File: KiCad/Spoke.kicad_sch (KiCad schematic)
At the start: 130 parts, among them J1 B2B-PH-K-S, J10 BL-A, J11 BL-C, J12 Amphenol 132289, J2 BAT+, J3 BAT-, J4 GCT USB4105/USB4110, J5 CHG+, J6 CHG-, J7 PLS-1x3, J8 PLS-1x6, J9 PLS-1x3, Q1 AO3407A, Q2 AO3400, Q3 AO3400, Q4 AO3400, SW1 PWR, SW2 OK/UP, SW3 ESC/DN, SW4 OK/UP, SW5 ESC/DN, SW6 BOOT, U1 SP0503BAHTG, U2 TP4056, U3 CP2102N-A02-GQFN28, U4 LM3671MF-3.3, U5 74HC4052PW, U6 STM32F103C8T6, U7 LSM303DLHC, X1 8MHz

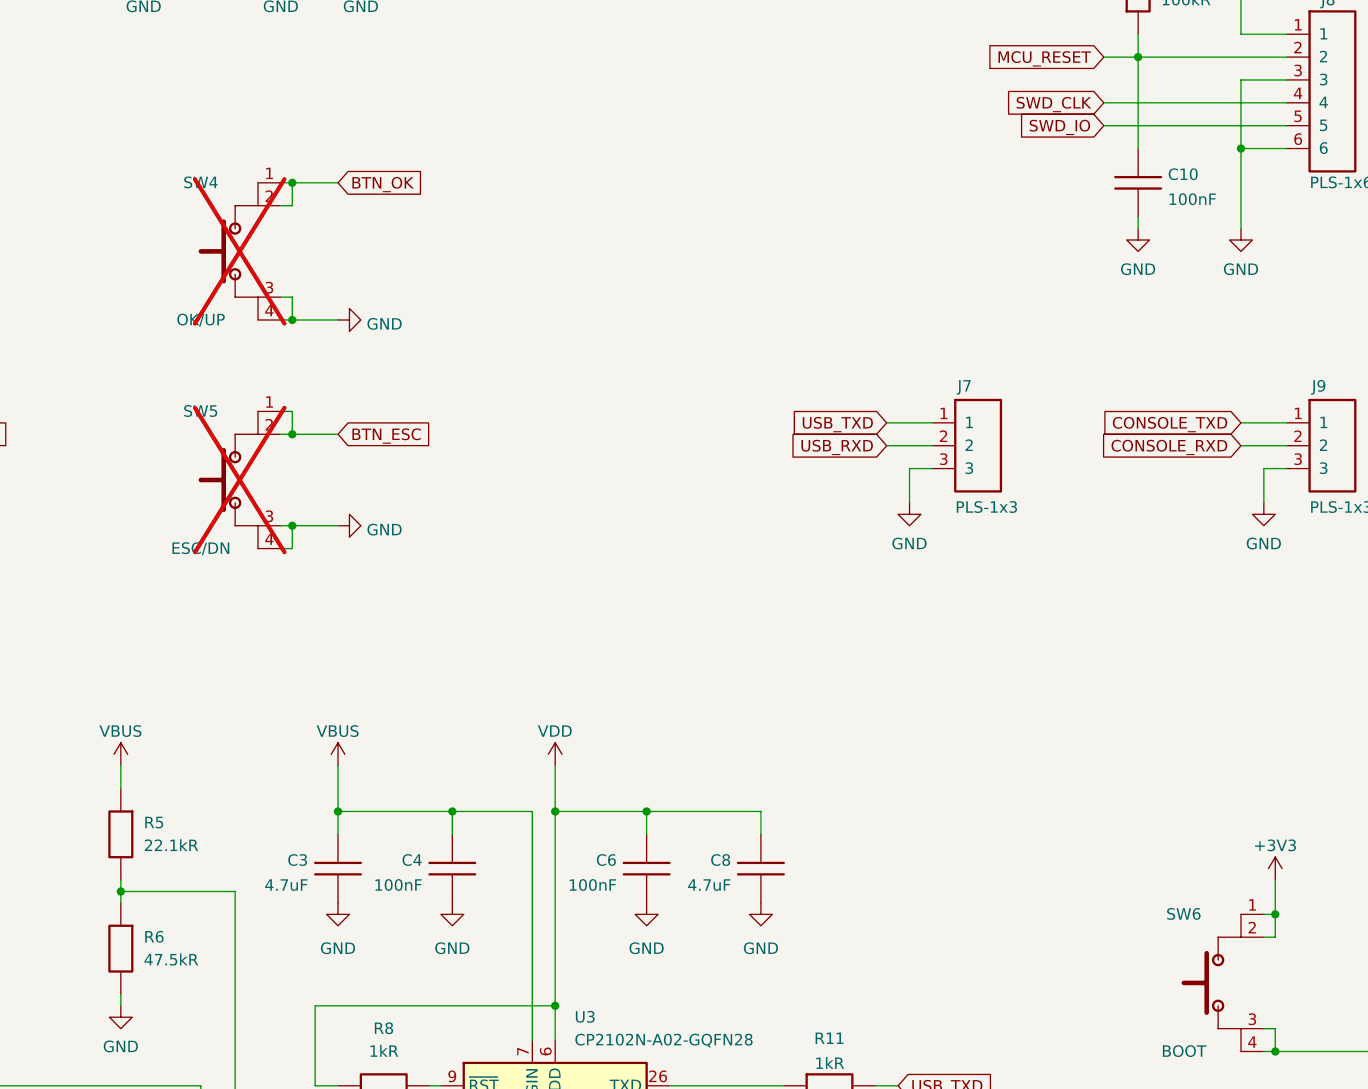
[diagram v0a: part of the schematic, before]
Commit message: Remove unused switches, arrangement
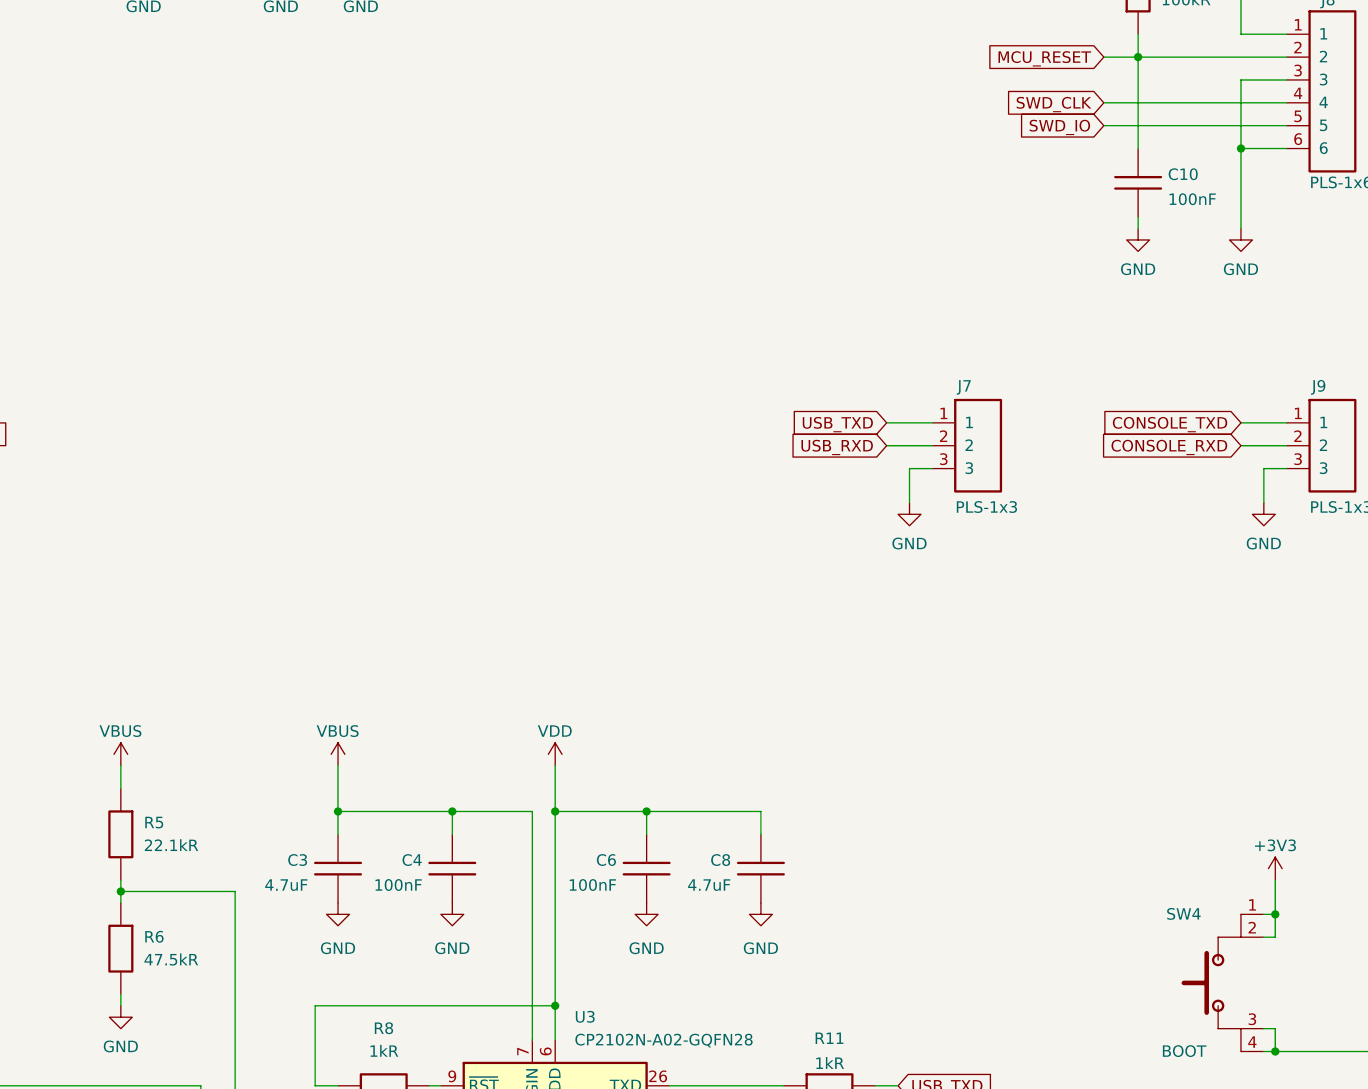
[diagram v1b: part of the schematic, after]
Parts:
- removed SW4: OK/UP, Spoke:Button_6x6, symbol Spoke:Button-SPST-NO
- removed SW5: ESC/DN, Spoke:Button_6x6, symbol Spoke:Button-SPST-NO
- renumbered SW6 to SW4

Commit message: Replace LEDs by 3 mm
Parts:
- D2, D3, D4: footprint Spoke:LED1206 -> Spoke:LED_3mm
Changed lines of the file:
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@@
 			)
 		)
-		(property "Footprint" "Spoke:LED1206"
+		(property "Footprint" "Spoke:LED_3mm"
 			(at 346.71 203.2 0)
 			(effects
@@
 			)
 		)
-		(property "Footprint" "Spoke:LED1206"
+		(property "Footprint" "Spoke:LED_3mm"
 			(at 134.62 349.25 0)
 			(effects
@@
 			)
 		)
-		(property "Footprint" "Spoke:LED1206"
+		(property "Footprint" "Spoke:LED_3mm"
 			(at 346.71 215.9 0)
 			(effects

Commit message: Start routing
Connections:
- net at J4.A7 (D-), J4.B7 (D-), U3.5 (D-): now also U1.3 (K); no longer U1.2 (K)
- net at J4.A6 (D+), J4.B6 (D+), U3.4 (D+): now also U1.2 (K); no longer U1.3 (K)
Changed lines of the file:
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@@
 	)
 	(junction
-		(at 95.25 246.38)
-		(diameter 0)
-		(color 0 0 0 0)
-	)
-	(junction
 		(at 298.45 45.72)
 		(diameter 0)
@@
 	)
 	(junction
+		(at 95.25 243.84)
+		(diameter 0)
+		(color 0 0 0 0)
+	)
+	(junction
 		(at 331.47 60.96)
 		(diameter 0)
@@
 	)
 	(junction
-		(at 92.71 243.84)
-		(diameter 0)
-		(color 0 0 0 0)
-	)
-	(junction
 		(at 115.57 88.9)
 		(diameter 0)
@@
 		(color 0 0 0 0)
 	)
+	(junction
+		(at 92.71 246.38)
+		(diameter 0)
+		(color 0 0 0 0)
+	)
 	(no_connect
 		(at 149.86 289.56)
@@
 	(wire
 		(pts
-			(xy 62.23 243.84) (xy 92.71 243.84)
-		)
-		(stroke
-			(width 0)
-			(type default)
-		)
-	)
-	(wire
-		(pts
 			(xy 488.95 194.31) (xy 492.76 194.31)
 		)
@@
 	(wire
 		(pts
-			(xy 95.25 246.38) (xy 124.46 246.38)
+			(xy 62.23 246.38) (xy 92.71 246.38)
 		)
 		(stroke
@@
 	(wire
 		(pts
-			(xy 92.71 243.84) (xy 92.71 251.46)
-		)
-		(stroke
-			(width 0)
-			(type default)
-		)
-	)
-	(wire
-		(pts
 			(xy 85.09 349.25) (xy 97.79 349.25)
 		)
@@
 	(wire
 		(pts
-			(xy 95.25 246.38) (xy 95.25 251.46)
-		)
-		(stroke
-			(width 0)
-			(type default)
-		)
-	)
-	(wire
-		(pts
 			(xy 339.09 132.08) (xy 339.09 134.62)
 		)
@@
 	(wire
 		(pts
-			(xy 62.23 246.38) (xy 95.25 246.38)
-		)
-		(stroke
-			(width 0)
-			(type default)
-		)
-	)
-	(wire
-		(pts
 			(xy 129.54 374.65) (xy 129.54 369.57)
 		)
@@
 	(wire
 		(pts
+			(xy 92.71 246.38) (xy 124.46 246.38)
+		)
+		(stroke
+			(width 0)
+			(type default)
+		)
+	)
+	(wire
+		(pts
 			(xy 459.74 182.88) (xy 459.74 212.09)
 		)
@@
 	(wire
 		(pts
-			(xy 92.71 243.84) (xy 124.46 243.84)
+			(xy 62.23 243.84) (xy 95.25 243.84)
 		)
 		(stroke
@@
 	(wire
 		(pts
+			(xy 92.71 246.38) (xy 92.71 251.46)
+		)
+		(stroke
+			(width 0)
+			(type default)
+		)
+	)
+	(wire
+		(pts
 			(xy 354.33 71.12) (xy 358.14 71.12)
 		)
@@
 	(wire
 		(pts
+			(xy 95.25 243.84) (xy 95.25 251.46)
+		)
+		(stroke
+			(width 0)
+			(type default)
+		)
+	)
+	(wire
+		(pts
 			(xy 48.26 50.8) (xy 48.26 45.72)
 		)
@@
 		)
 		(stroke
+			(width 0)
+			(type default)
+		)
+	)
+	(wire
+		(pts
+			(xy 95.25 243.84) (xy 124.46 243.84)
+		)
+		(stroke

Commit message: Replace DCDC caps by Ceramic 10 uF
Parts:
- removed C13, C7: 47uF, Spoke:C_tantA, symbol Spoke:C-Polar
- added C13, C7: 10uF, Spoke:C1206, symbol Spoke:C
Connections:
- net +3V3: now also C13.2
- net GND: now also C13.1, C7.1
- net VCC: now also C7.2
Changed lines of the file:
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@@
 	)
 	(symbol
-		(lib_id "Spoke:C-Polar")
-		(at 158.75 52.07 270)
+		(lib_id "power:GND")
+		(at 39.37 269.24 0)
 		(unit 1)
 		(exclude_from_sim no)
@@
 		(dnp no)
 		(fields_autoplaced yes)
-		(property "Reference" "C7"
-			(at 163.83 53.7209 90)
+		(property "Reference" "#PWR01"
+			(at 39.37 275.59 0)
 			(effects
 				(font
 					(size 1.27 1.27)
 				)
-				(justify left)
+				(hide yes)
 			)
 		)
-		(property "Value" "47uF"
-			(at 163.83 56.2609 90)
+		(property "Value" "GND"
+			(at 39.37 273.8025 0)
 			(effects
 				(font
 					(size 1.27 1.27)
 				)
-				(justify left)
 			)
 		)
-		(property "Footprint" "Spoke:C_tantA"
-			(at 171.45 52.07 0)
+		(property "Footprint" ""
+			(at 39.37 269.24 0)
 			(effects
 				(font
@@
 		)
 		(property "Datasheet" ""
-			(at 171.45 52.07 0)
+			(at 39.37 269.24 0)
 			(effects
 				(font
@@
 		)
 		(property "Description" ""
-			(at 158.75 52.07 0)
+			(at 39.37 269.24 0)
 			(effects
 				(font
 					(size 1.27 1.27)
 				)
-				(hide yes)
 			)
 		)
 		(pin "1"
 		)
-		(pin "2"
-		)
 		(instances
 			(project "Spoke"
 				(path "/e63e39d7-6ac0-4ffd-8aa3-1841a4541b55"
-					(reference "C7")
+					(reference "#PWR01")
 					(unit 1)
 				)
@@
 	)
 	(symbol
-		(lib_id "power:GND")
-		(at 39.37 269.24 0)
+		(lib_id "Spoke:C")
+		(at 158.75 59.69 90)
 		(unit 1)
 		(exclude_from_sim no)
@@
 		(dnp no)
 		(fields_autoplaced yes)
-		(property "Reference" "#PWR01"
-			(at 39.37 275.59 0)
+		(property "Reference" "C7"
+			(at 155.4481 54.9715 90)
 			(effects
 				(font
 					(size 1.27 1.27)
 				)
-				(hide yes)
+				(justify left)
 			)
 		)
-		(property "Value" "GND"
-			(at 39.37 273.8025 0)
+		(property "Value" "10uF"
+			(at 155.4481 57.7466 90)
 			(effects
 				(font
 					(size 1.27 1.27)
 				)
+				(justify left)
 			)
 		)
-		(property "Footprint" ""
-			(at 39.37 269.24 0)
+		(property "Footprint" "Spoke:C1206"
+			(at 146.05 59.69 0)
 			(effects
 				(font
@@
 		)
 		(property "Datasheet" ""
-			(at 39.37 269.24 0)
+			(at 146.05 59.69 0)
 			(effects
 				(font
@@
 		)
 		(property "Description" ""
-			(at 39.37 269.24 0)
+			(at 158.75 59.69 0)
 			(effects
 				(font
@@
 		(pin "1"
 		)
+		(pin "2"
+		)
 		(instances
 			(project "Spoke"
 				(path "/e63e39d7-6ac0-4ffd-8aa3-1841a4541b55"
-					(reference "#PWR01")
+					(reference "C7")
 					(unit 1)
 				)
@@
 	)
 	(symbol
+		(lib_id "Spoke:C")
+		(at 243.84 59.69 90)
+		(unit 1)
+		(exclude_from_sim no)
+		(in_bom yes)
+		(on_board yes)
+		(dnp no)
+		(fields_autoplaced yes)
+		(property "Reference" "C13"
+			(at 240.5381 54.9715 90)
+			(effects
+				(font
+					(size 1.27 1.27)
+				)
+				(justify left)
+			)
+		)
+		(property "Value" "10uF"
+			(at 240.5381 57.7466 90)
+			(effects
+				(font
+					(size 1.27 1.27)
+				)
+				(justify left)
+			)
+		)
+		(property "Footprint" "Spoke:C1206"
+			(at 231.14 59.69 0)
+			(effects
+				(font
+					(size 1.27 1.27)
+				)
+				(hide yes)
+			)
+		)
+		(property "Datasheet" ""
+			(at 231.14 59.69 0)
+			(effects
+				(font
+					(size 1.27 1.27)
+				)
+				(hide yes)
+			)
+		)
+		(property "Description" ""
+			(at 243.84 59.69 0)
+			(effects
+				(font
+					(size 1.27 1.27)
+				)
+			)
+		)
+		(pin "1"
+		)
+		(pin "2"
+		)
+		(instances
+			(project "Spoke"
+				(path "/e63e39d7-6ac0-4ffd-8aa3-1841a4541b55"
+					(reference "C13")
+					(unit 1)
+				)
+			)
+		)
+	)
+	(symbol
 		(lib_id "Spoke:R")
 		(at 236.22 294.64 0)
@@
 					(unit 1)
 				)
-			)
-		)
-	)
-	(symbol
-		(lib_id "Spoke:C-Polar")
-		(at 243.84 52.07 270)
-		(unit 1)
-		(exclude_from_sim no)
-		(in_bom yes)
-		(on_board yes)
-		(dnp no)
-		(fields_autoplaced yes)
-		(property "Reference" "C13"
-			(at 248.92 53.7209 90)
-			(effects
-				(font
-					(size 1.27 1.27)
-				)
-				(justify left)
-			)
-		)
-		(property "Value" "47uF"
-			(at 248.92 56.2609 90)
-			(effects
-				(font
-					(size 1.27 1.27)
-				)
-				(justify left)
-			)
-		)
-		(property "Footprint" "Spoke:C_tantA"
-			(at 256.54 52.07 0)
-			(effects
-				(font
-					(size 1.27 1.27)
-				)
-				(hide yes)
-			)
-		)
-		(property "Datasheet" ""
-			(at 256.54 52.07 0)
-			(effects
-				(font
-					(size 1.27 1.27)
-				)
-				(hide yes)
-			)
-		)
-		(property "Description" ""
-			(at 243.84 52.07 0)
-			(effects
-				(font
-					(size 1.27 1.27)
-				)
-				(hide yes)
-			)
-		)
-		(pin "1"
-		)
-		(pin "2"
-		)
-		(instances
-			(project ""
-				(path "/e63e39d7-6ac0-4ffd-8aa3-1841a4541b55"
-					(reference "C13")
-					(unit 1)
-				)

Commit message: Route USB-UART
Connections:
- net USB_DP: now reaches J4.A6 (D+), J4.B6 (D+), U1.2 (K), U3.4 (D+)
- net USB_DN: now reaches J4.A7 (D-), J4.B7 (D-), U1.3 (K), U3.5 (D-)
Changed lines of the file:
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@@
+		)
+	)
+	(label "USB_DN"
+		(at 101.6 243.84 0)
+		(effects
+			(font
+				(size 1.27 1.27)
+			)
+			(justify left bottom)
 		)
 	)
@@
 		(effects
 			(font
+				(size 1.27 1.27)
+			)
+			(justify left bottom)
+		)
+	)
+	(label "USB_DP"
+		(at 101.6 246.38 0)
+		(effects
+			(font

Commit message: Add C14
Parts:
- added C14: 47uF, Spoke:C_tantA, symbol Spoke:C-Polar
- renumbered C14 to C15, C15 to C16, C16 to C17, C17 to C18, C18 to C19, C19 to C20, C20 to C21, C21 to C22, C22 to C23, C23 to C24, C24 to C25, C25 to C26, C26 to C27, C27 to C28, C28 to C29, C29 to C30, C30 to C31, C31 to C32, C32 to C33
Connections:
- net +3V3: now also C14.1
- net GND: now also C14.2
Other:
- moved on the sheet: C16, C17, C18, C20

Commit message: Add TP1, TP2
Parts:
- added TP1, TP2: Pad-Round, Spoke:Pad_round, symbol Spoke:Pad-Round
- renumbered TP8 to TP10, TP9 to TP11, TP10 to TP12, TP11 to TP13, TP12 to TP14, TP13 to TP15, TP14 to TP16, TP15 to TP17, TP16 to TP18, TP1 to TP3, TP2 to TP4, TP3 to TP5, TP4 to TP6, TP5 to TP7, TP6 to TP8, TP7 to TP9
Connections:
- net MUX_BLE_USB: now also TP2.1
- net VDD: now also TP1.1
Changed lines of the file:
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@@
 	)
 	(junction
+		(at 203.2 334.01)
+		(diameter 0)
+		(color 0 0 0 0)
+	)
+	(junction
 		(at 91.44 58.42)
 		(diameter 0)
@@
 	)
 	(junction
+		(at 160.02 198.12)
+		(diameter 0)
+		(color 0 0 0 0)
+	)
+	(junction
 		(at 414.02 335.28)
 		(diameter 0)
@@
 	(wire
 		(pts
-			(xy 203.2 330.2) (xy 203.2 349.25)
+			(xy 203.2 330.2) (xy 203.2 334.01)
 		)
 		(stroke
@@
 	(wire
 		(pts
+			(xy 201.93 334.01) (xy 203.2 334.01)
+		)
+		(stroke
+			(width 0)
+			(type default)
+		)
+	)
+	(wire
+		(pts
 			(xy 92.71 246.38) (xy 124.46 246.38)
 		)
@@
 	(wire
 		(pts
+			(xy 203.2 334.01) (xy 203.2 349.25)
+		)
+		(stroke
+			(width 0)
+			(type default)
+		)
+	)
+	(wire
+		(pts
 			(xy 106.68 100.33) (xy 106.68 104.14)
 		)
@@
 		(on_board yes)
 		(dnp no)
-		(property "Reference" "TP3"
+		(property "Reference" "TP5"
 			(at 303.53 325.12 0)
 			(effects
@@
 			(project "Spoke"
 				(path "/e63e39d7-6ac0-4ffd-8aa3-1841a4541b55"
-					(reference "TP3")
+					(reference "TP5")
 					(unit 1)
 				)
@@
 		(on_board yes)
 		(dnp no)
-		(property "Reference" "TP1"
+		(property "Reference" "TP3"
 			(at 194.31 356.87 0)
 			(effects
@@
 			(project "Spoke"
 				(path "/e63e39d7-6ac0-4ffd-8aa3-1841a4541b55"
-					(reference "TP1")
+					(reference "TP3")
 					(unit 1)
 				)
@@
 		(on_board yes)
 		(dnp no)
-		(property "Reference" "TP16"
+		(property "Reference" "TP18"
 			(at 483.87 193.04 0)
 			(effects
@@
 			(project "Spoke"
 				(path "/e63e39d7-6ac0-4ffd-8aa3-1841a4541b55"
-					(reference "TP16")
+					(reference "TP18")
 					(unit 1)
 				)
@@
 	)
 	(symbol
+		(lib_id "Spoke:Pad-Round")
+		(at 160.02 198.12 270)
+		(mirror x)
+		(unit 1)
+		(exclude_from_sim no)
+		(in_bom yes)
+		(on_board yes)
+		(dnp no)
+		(property "Reference" "TP1"
+			(at 160.02 190.5 0)
+			(effects
+				(font
+					(size 1.27 1.27)
+				)
+			)
+		)
+		(property "Value" "Pad-Round"
+			(at 157.48 193.04 0)
+			(effects
+				(font
+					(size 1.27 1.27)
+				)
+				(hide yes)
+			)
+		)
+		(property "Footprint" "Spoke:Pad_round"
+			(at 160.02 198.12 0)
+			(effects
+				(font
+					(size 1.27 1.27)
+				)
+				(hide yes)
+			)
+		)
+		(property "Datasheet" ""
+			(at 160.02 198.12 0)
+			(effects
+				(font
+					(size 1.27 1.27)
+				)
+				(hide yes)
+			)
+		)
+		(property "Description" ""
+			(at 160.02 198.12 0)
+			(effects
+				(font
+					(size 1.27 1.27)
+				)
+				(hide yes)
+			)
+		)
+		(pin "1"
+		)
+		(instances
+			(project "Spoke"
+				(path "/e63e39d7-6ac0-4ffd-8aa3-1841a4541b55"
+					(reference "TP1")
+					(unit 1)
+				)
+			)
+		)
+	)
+	(symbol
 		(lib_id "power:GND")
 		(at 113.03 208.28 0)
@@
 		(on_board yes)
 		(dnp no)
-		(property "Reference" "TP10"
+		(property "Reference" "TP12"
 			(at 406.4 355.6 0)
 			(effects
@@
 			(project "Spoke"
 				(path "/e63e39d7-6ac0-4ffd-8aa3-1841a4541b55"
-					(reference "TP10")
+					(reference "TP12")
 					(unit 1)
 				)
@@
 		(on_board yes)
 		(dnp no)
-		(property "Reference" "TP11"
+		(property "Reference" "TP13"
 			(at 472.44 298.45 0)
 			(effects
@@
 			(project ""
 				(path "/e63e39d7-6ac0-4ffd-8aa3-1841a4541b55"
-					(reference "TP11")
+					(reference "TP13")
 					(unit 1)
 				)
@@
 		(on_board yes)
 		(dnp no)
-		(property "Reference" "TP14"
+		(property "Reference" "TP16"
 			(at 480.06 193.04 0)
 			(effects
@@
 			(project "Spoke"
 				(path "/e63e39d7-6ac0-4ffd-8aa3-1841a4541b55"
-					(reference "TP14")
+					(reference "TP16")
 					(unit 1)
 				)
@@
 		(on_board yes)
 		(dnp no)
-		(property "Reference" "TP8"
+		(property "Reference" "TP10"
 			(at 406.4 347.98 0)
 			(effects
@@
 			(project "Spoke"
 				(path "/e63e39d7-6ac0-4ffd-8aa3-1841a4541b55"
-					(reference "TP8")
+					(reference "TP10")
 					(unit 1)
 				)
@@
 	)
 	(symbol
+		(lib_id "Spoke:Pad-Round")
+		(at 201.93 334.01 0)
+		(mirror y)
+		(unit 1)
+		(exclude_from_sim no)
+		(in_bom yes)
+		(on_board yes)
+		(dnp no)
+		(property "Reference" "TP2"
+			(at 194.31 334.01 0)
+			(effects
+				(font
+					(size 1.27 1.27)
+				)
+			)
+		)
+		(property "Value" "Pad-Round"
+			(at 196.85 336.55 0)
+			(effects
+				(font
+					(size 1.27 1.27)
+				)
+				(hide yes)
+			)
+		)
+		(property "Footprint" "Spoke:Pad_round"
+			(at 201.93 334.01 0)
+			(effects
+				(font
+					(size 1.27 1.27)
+				)
+				(hide yes)
+			)
+		)
+		(property "Datasheet" ""
+			(at 201.93 334.01 0)
+			(effects
+				(font
+					(size 1.27 1.27)
+				)
+				(hide yes)
+			)
+		)
+		(property "Description" ""
+			(at 201.93 334.01 0)
+			(effects
+				(font
+					(size 1.27 1.27)
+				)
+				(hide yes)
+			)
+		)
+		(pin "1"
+		)
+		(instances
+			(project "Spoke"
+				(path "/e63e39d7-6ac0-4ffd-8aa3-1841a4541b55"
+					(reference "TP2")
+					(unit 1)
+				)
+			)
+		)
+	)
+	(symbol
 		(lib_id "Spoke:R")
 		(at 327.66 354.33 270)
@@
 		(on_board yes)
 		(dnp no)
-		(property "Reference" "TP2"
+		(property "Reference" "TP4"
 			(at 297.18 325.12 0)
 			(effects
@@
 			(project "Spoke"
 				(path "/e63e39d7-6ac0-4ffd-8aa3-1841a4541b55"
-					(reference "TP2")
+					(reference "TP4")
 					(unit 1)
 				)
@@
 		(on_board yes)
 		(dnp no)
-		(property "Reference" "TP6"
+		(property "Reference" "TP8"
 			(at 317.5 347.98 0)
 			(effects
@@
 			(project "Spoke"
 				(path "/e63e39d7-6ac0-4ffd-8aa3-1841a4541b55"
-					(reference "TP6")
+					(reference "TP8")
 					(unit 1)
 				)
@@
 		(on_board yes)
 		(dnp no)
-		(property "Reference" "TP5"
+		(property "Reference" "TP7"
 			(at 317.5 345.44 0)
 			(effects
@@
 			(project "Spoke"
 				(path "/e63e39d7-6ac0-4ffd-8aa3-1841a4541b55"
-					(reference "TP5")
+					(reference "TP7")
 					(unit 1)
 				)
@@
 		(on_board yes)
 		(dnp no)
-		(property "Reference" "TP12"
+		(property "Reference" "TP14"
 			(at 476.25 193.04 0)
 			(effects
@@
 			(project "Spoke"
 				(path "/e63e39d7-6ac0-4ffd-8aa3-1841a4541b55"
-					(reference "TP12")
+					(reference "TP14")
 					(unit 1)
 				)
@@
 		(on_board yes)
 		(dnp no)
-		(property "Reference" "TP9"
+		(property "Reference" "TP11"
 			(at 406.4 350.52 0)
 			(effects
@@
 			(project "Spoke"
 				(path "/e63e39d7-6ac0-4ffd-8aa3-1841a4541b55"
-					(reference "TP9")
+					(reference "TP11")
 					(unit 1)
 				)
@@
 		(on_board yes)
 		(dnp no)
-		(property "Reference" "TP7"
+		(property "Reference" "TP9"
 			(at 317.5 350.52 0)
 			(effects
@@
 			(project "Spoke"
 				(path "/e63e39d7-6ac0-4ffd-8aa3-1841a4541b55"
-					(reference "TP7")
+					(reference "TP9")
 					(unit 1)
 				)
@@
 		(on_board yes)
 		(dnp no)
-		(property "Reference" "TP15"
+		(property "Reference" "TP17"
 			(at 482.6 298.45 0)
 			(effects
@@
 			(project ""
 				(path "/e63e39d7-6ac0-4ffd-8aa3-1841a4541b55"
-					(reference "TP15")
+					(reference "TP17")
 					(unit 1)
 				)
@@
 		(on_board yes)
 		(dnp no)
-		(property "Reference" "TP13"
+		(property "Reference" "TP15"
 			(at 477.52 298.45 0)
 			(effects
@@
 			(project ""
 				(path "/e63e39d7-6ac0-4ffd-8aa3-1841a4541b55"
-					(reference "TP13")
+					(reference "TP15")
 					(unit 1)
 				)
@@
 		(on_board yes)
 		(dnp no)
-		(property "Reference" "TP4"
+		(property "Reference" "TP6"
 			(at 317.5 342.9 0)
 			(effects
@@
 			(project "Spoke"
 				(path "/e63e39d7-6ac0-4ffd-8aa3-1841a4541b55"
-					(reference "TP4")
+					(reference "TP6")
 					(unit 1)
 				)

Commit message: Update SCH with notes, add R23
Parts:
- added R23: 0R, Spoke:R0603, symbol Spoke:R
- J5: value CHG+ -> USB+
- J6: value CHG- -> USB-
- renumbered R23 to R24, R24 to R25, R25 to R26, R26 to R28, R28 to R29, R29 to R30, R30 to R31, R31 to R32, R32 to R33, R33 to R34, R34 to R35, R35 to R36, R36 to R37, R37 to R38, R38 to R39
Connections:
- net MUX_BLE_USB: now also R23.2
- net BLE_WKP_SLP: now reaches A1.7 (WAKEUP/SLEEP), R29.1, TP6.1
- net BLE_WKP_SLP: now also R23.1
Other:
- moved on the sheet: A1, C21, C23, C24, R24, R28, R29, R30, R31, R32, R33, TP10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
